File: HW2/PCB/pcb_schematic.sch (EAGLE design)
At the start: 0 parts

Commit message: Started the schematic. Need to add nets.
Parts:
- added C1, C2, C3, C4: (no value), pcb_library:C-US025-025X050
- added C5, C6: (no value), pcb_library:CPOL-USB45181A
- added J1: USB-MB-H, pcb_library:USB-MB-H
- added LED1, LED2: (no value), pcb_library:LED3MM
- added U$1: SLIDE_SWITCH, pcb_library:SLIDE_SWITCH
- added U$2: MCP1702, pcb_library:MCP1702
- added U$3: PIC32MX250F128B, pcb_library:PIC32MX250F128B
- added U$4: PICKIT, pcb_library:PICKIT
- added U$5: J3, pcb_library:J3
- added U$6: J4, pcb_library:J4
- added U$7: 8MHZ, pcb_library:8MHZ

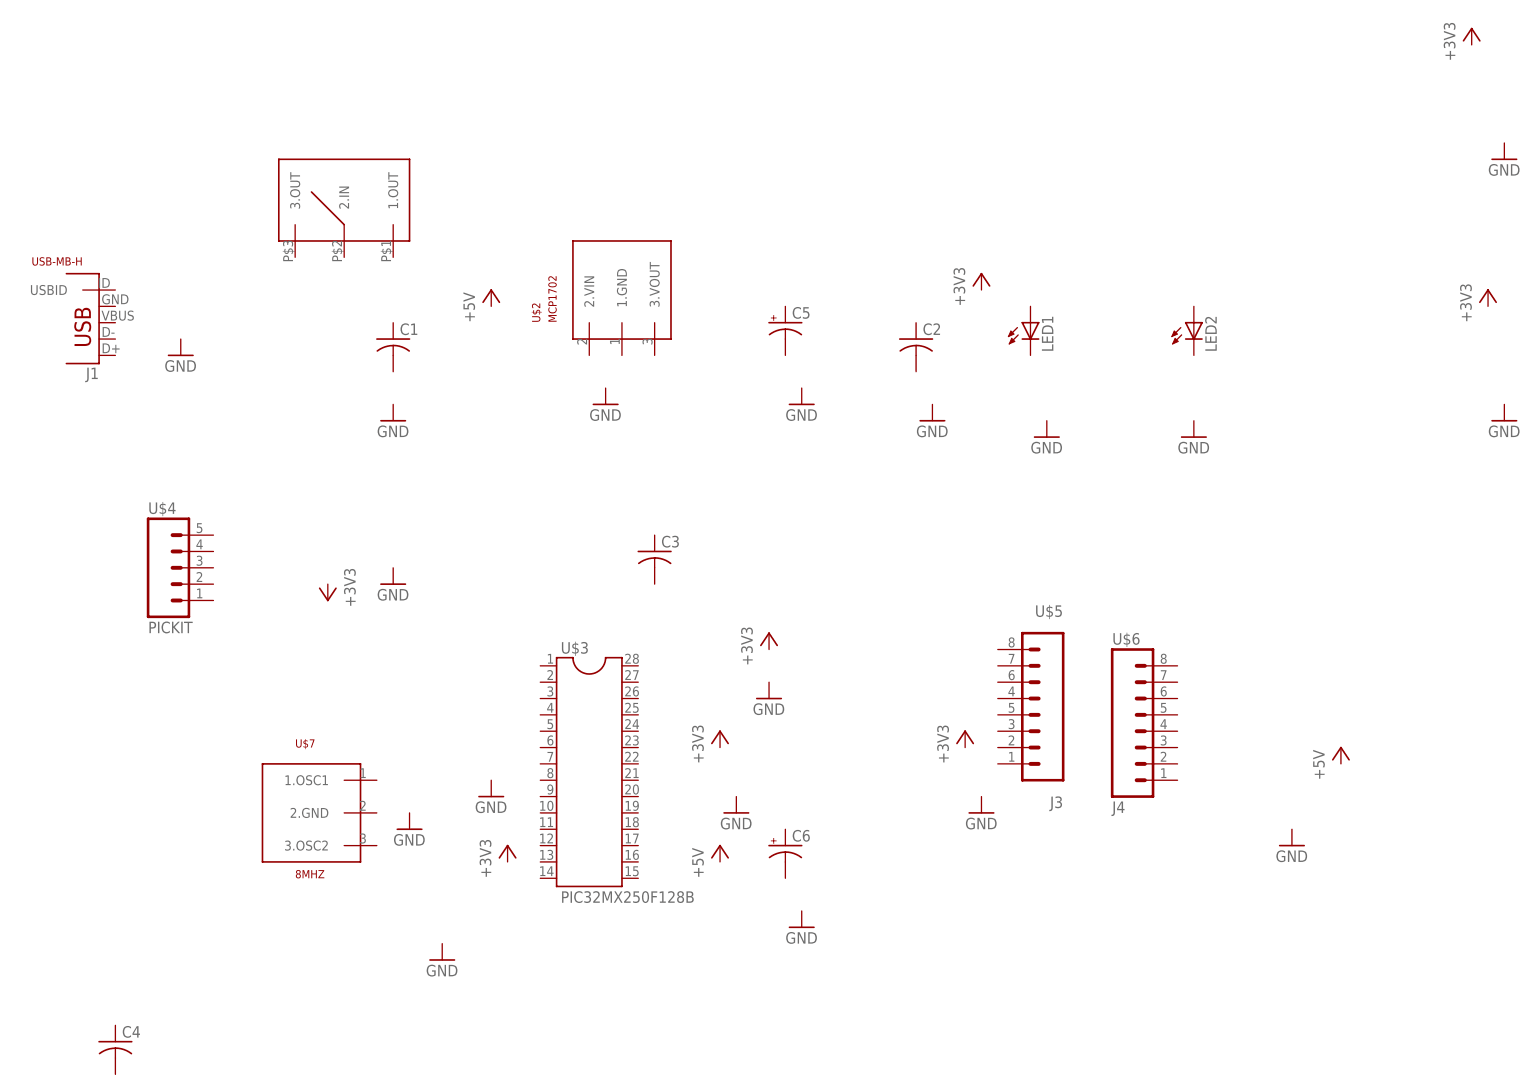
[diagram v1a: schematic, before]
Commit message: Finished a good bit of the schematic.
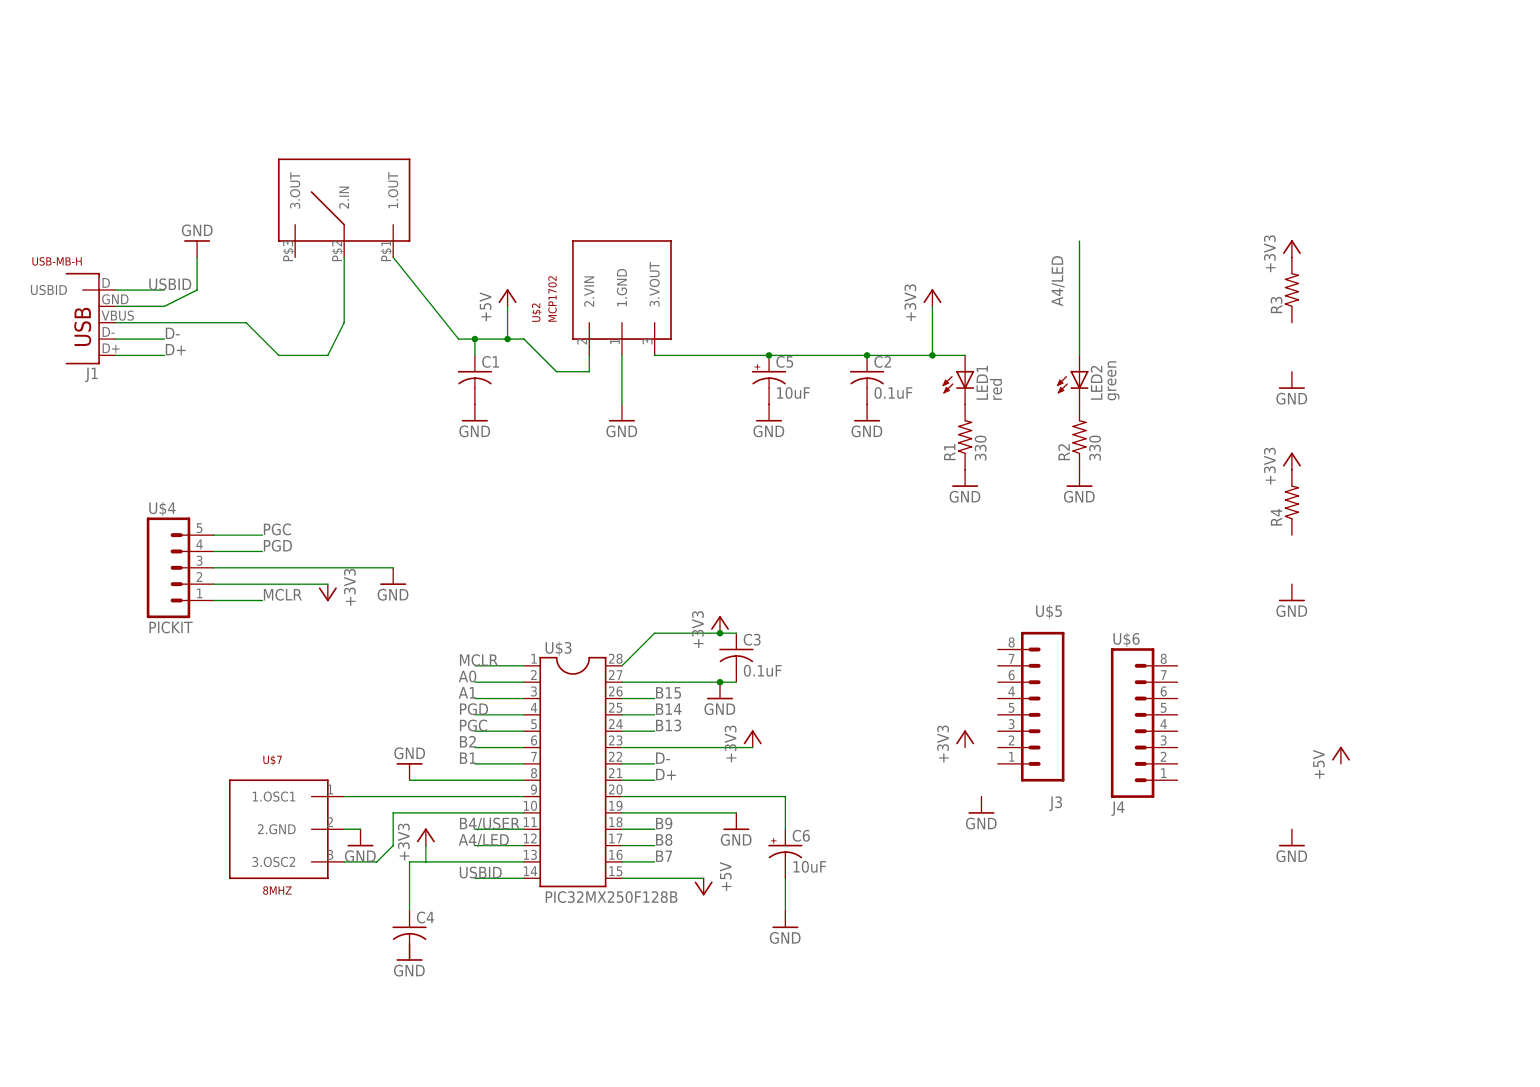
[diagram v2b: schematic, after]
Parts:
- added R1, R2: 330, pcb_library:R-US_0204/7
- added R3, R4: (no value), pcb_library:R-US_0204/7
- C2, C3: value (none) -> 0.1uF
- C5, C6: value (none) -> 10uF
- LED1: value (none) -> red
- LED2: value (none) -> green
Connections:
- new net +3V3: C2.1, C3.1, C4.1, C5.+, LED1.A, R3.2, R4.2, U$2.3.VOUT, U$3.13.VDD, U$3.23.VUSB3V3, U$3.28.AVDD, U$4.2.3V3
- new net +5V: C1.1, U$1.1.OUT, U$2.2.VIN, U$3.15.VBUS
- new net A0: U$3.2.A0
- new net A1: U$3.3.A1
- new net A4/LED: LED2.A, U$3.12.A4/LED
- new net B1: U$3.7.B3
- new net B13: U$3.24.B13
- new net B14: U$3.25.B14
- new net B15: U$3.26.B15
- new net B2: U$3.6.B2
- new net B4/USER: U$3.11.B4/USER
- new net B7: U$3.16.B7
- new net B8: U$3.17.B8
- new net B9: U$3.18.B9
- new net D+: J1.D+, U$3.21.D+/B10
- new net D-: J1.D-, U$3.22.D-/B11
- new net GND: C1.2, C2.2, C3.2, C5.-, C6.-, J1.GND, R1.1, R2.1, U$2.1.GND, U$3.19.VSS, U$3.27.AVSS, U$3.8.GND, U$4.3.GND, U$7.2.GND
- new net MCLR: U$3.1.MCLR, U$4.1.MCLR
- new net N$1: J1.VBUS, U$1.2.IN
- new net N$14: C6.+, U$3.20.VCAP
- new net N$2: LED1.C, R1.2
- new net N$3: LED2.C, R2.2
- new net N$4: U$3.9.OSC1, U$7.1.OSC1
- new net N$5: U$3.10.OSC2, U$7.3.OSC2
- new net PGC: U$3.5.PGC, U$4.5.PGC
- new net PGD: U$3.4.PGD, U$4.4.PGD
- new net USBID: J1.USBID, U$3.14.USBID/B5
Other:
- moved on the sheet: C1, C2, C3, C4, C5, LED1, LED2, U$3, U$7

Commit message: Finished schematic minus the buttons. Not sure what to do about those still.
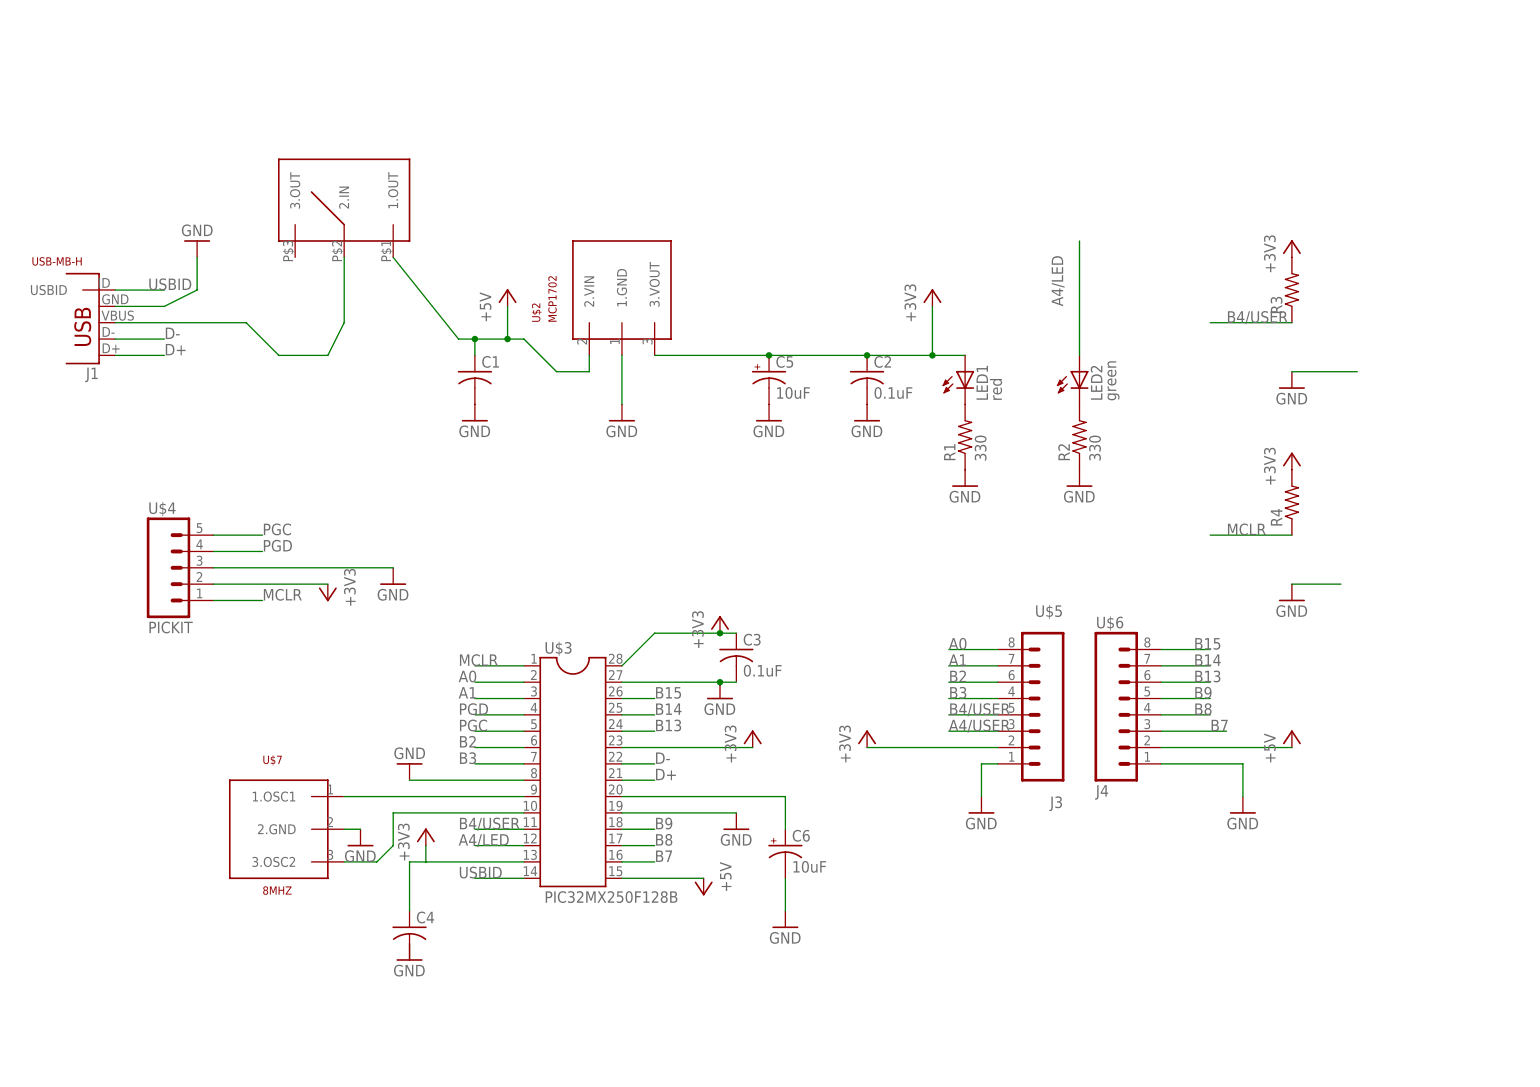
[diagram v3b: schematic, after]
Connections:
- removed net B1: U$3.7.B3
- new net A4/USER: U$5.3.A4/LED
- new net B3: U$3.7.B3, U$5.4.B4/USER
- net +3V3: now also U$5.2.3V3
- net +5V: now also U$6.2.5V
- net A0: now also U$5.8.A0
- net A1: now also U$5.7.A1
- net B13: now also U$6.6.B13
- net B14: now also U$6.7.B14
- net B15: now also U$6.8.B15
- net B2: now also U$5.5.B3
- net B4/USER: now also R3.1, U$5.5
- net B7: now also U$6.3.B7
- net B8: now also U$6.4.B8
- net B9: now also U$6.5.B9
- net GND: now also U$5.1.GND, U$6.1.GND
- net MCLR: now also R4.1
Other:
- moved on the sheet: U$6
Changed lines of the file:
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@@
 <instance part="U$4" gate="G$1" x="-66.04" y="33.02"/>
 <instance part="U$5" gate="G$1" x="71.12" y="12.7"/>
-<instance part="U$6" gate="G$1" x="86.36" y="7.62"/>
+<instance part="U$6" gate="G$1" x="83.82" y="10.16"/>
 <instance part="U$7" gate="G$1" x="-40.64" y="-7.62"/>
 <instance part="P+1" gate="1" x="-12.7" y="76.2"/>
-<instance part="P+2" gate="1" x="116.84" y="5.08"/>
+<instance part="P+2" gate="1" x="109.22" y="7.62"/>
 <instance part="P+3" gate="1" x="17.78" y="-17.78" rot="R180"/>
 <instance part="+3V1" gate="G$1" x="53.34" y="76.2"/>
 <instance part="+3V2" gate="G$1" x="109.22" y="83.82"/>
 <instance part="+3V3" gate="G$1" x="109.22" y="50.8"/>
-<instance part="+3V4" gate="G$1" x="58.42" y="7.62"/>
+<instance part="+3V4" gate="G$1" x="43.18" y="7.62"/>
 <instance part="+3V5" gate="G$1" x="25.4" y="7.62"/>
 <instance part="+3V6" gate="G$1" x="20.32" y="25.4"/>
@@
 <instance part="GND8" gate="1" x="109.22" y="60.96"/>
 <instance part="GND9" gate="1" x="109.22" y="27.94"/>
-<instance part="GND10" gate="1" x="109.22" y="-10.16"/>
+<instance part="GND10" gate="1" x="101.6" y="-5.08"/>
 <instance part="GND11" gate="1" x="60.96" y="-5.08"/>
 <instance part="GND12" gate="1" x="20.32" y="12.7"/>
@@
 <pinref part="GND13" gate="1" pin="GND"/>
 </segment>
+<segment>
+<pinref part="U$5" gate="G$1" pin="1.GND"/>
+<wire x1="63.5" y1="2.54" x2="60.96" y2="2.54" width="0.1524" layer="91"/>
+<pinref part="GND11" gate="1" pin="GND"/>
+<wire x1="60.96" y1="2.54" x2="60.96" y2="-2.54" width="0.1524" layer="91"/>
+</segment>
+<segment>
+<pinref part="U$6" gate="G$1" pin="1.GND"/>
+<wire x1="88.9" y1="2.54" x2="101.6" y2="2.54" width="0.1524" layer="91"/>
+<wire x1="101.6" y1="2.54" x2="101.6" y2="-2.54" width="0.1524" layer="91"/>
+<pinref part="GND10" gate="1" pin="GND"/>
+</segment>
+<segment>
+<pinref part="GND8" gate="1" pin="GND"/>
+<wire x1="119.38" y1="63.5" x2="109.22" y2="63.5" width="0.1524" layer="91"/>
+</segment>
+<segment>
+<pinref part="GND9" gate="1" pin="GND"/>
+<wire x1="116.84" y1="30.48" x2="109.22" y2="30.48" width="0.1524" layer="91"/>
+</segment>
 </net>
 <net name="USBID" class="0">
@@
 <pinref part="P+3" gate="1" pin="+5V"/>
 </segment>
+<segment>
+<pinref part="U$6" gate="G$1" pin="2.5V"/>
+<wire x1="88.9" y1="5.08" x2="109.22" y2="5.08" width="0.1524" layer="91"/>
+<pinref part="P+2" gate="1" pin="+5V"/>
+</segment>
 </net>
 <net name="+3V3" class="0">
@@
 <wire x1="5.08" y1="5.08" x2="25.4" y2="5.08" width="0.1524" layer="91"/>
 </segment>
+<segment>
+<pinref part="U$5" gate="G$1" pin="2.3V3"/>
+<pinref part="+3V4" gate="G$1" pin="+3V3"/>
+<wire x1="63.5" y1="5.08" x2="43.18" y2="5.08" width="0.1524" layer="91"/>
+</segment>
 </net>
 <net name="N$2" class="0">
@@
 <label x="-20.32" y="17.78" size="1.778" layer="95"/>
 </segment>
+<segment>
+<pinref part="R4" gate="G$1" pin="1"/>
+<wire x1="96.52" y1="38.1" x2="109.22" y2="38.1" width="0.1524" layer="91"/>
+<label x="99.06" y="38.1" size="1.778" layer="95"/>
+</segment>
 </net>
 <net name="A0" class="0">
@@
 <label x="-20.32" y="15.24" size="1.778" layer="95"/>
 </segment>
+<segment>
+<pinref part="U$5" gate="G$1" pin="8.A0"/>
+<wire x1="55.88" y1="20.32" x2="63.5" y2="20.32" width="0.1524" layer="91"/>
+<label x="55.88" y="20.32" size="1.778" layer="95"/>
+</segment>
 </net>
 <net name="A1" class="0">
@@
 <label x="-20.32" y="12.7" size="1.778" layer="95"/>
 </segment>
+<segment>
+<pinref part="U$5" gate="G$1" pin="7.A1"/>
+<wire x1="55.88" y1="17.78" x2="63.5" y2="17.78" width="0.1524" layer="91"/>
+<label x="55.88" y="17.78" size="1.778" layer="95"/>
+</segment>
 </net>
 <net name="B2" class="0">
@@
 <label x="-20.32" y="5.08" size="1.778" layer="95"/>
 </segment>
-</net>
-<net name="B1" class="0">
-<segment>
-<pinref part="U$3" gate="G$1" pin="7.B3"/>
-<wire x1="-10.16" y1="2.54" x2="-17.78" y2="2.54" width="0.1524" layer="91"/>
-<label x="-20.32" y="2.54" size="1.778" layer="95"/>
+<segment>
+<pinref part="U$5" gate="G$1" pin="5.B3"/>
+<wire x1="55.88" y1="15.24" x2="63.5" y2="15.24" width="0.1524" layer="91"/>
+<label x="55.88" y="15.24" size="1.778" layer="95"/>
 </segment>
 </net>
@@
 <label x="-20.32" y="-7.62" size="1.778" layer="95"/>
 </segment>
+<segment>
+<pinref part="U$5" gate="G$1" pin="5"/>
+<wire x1="55.88" y1="10.16" x2="63.5" y2="10.16" width="0.1524" layer="91"/>
+<label x="55.88" y="10.16" size="1.778" layer="95"/>
+</segment>
+<segment>
+<pinref part="R3" gate="G$1" pin="1"/>
+<wire x1="96.52" y1="71.12" x2="109.22" y2="71.12" width="0.1524" layer="91"/>
+<label x="99.06" y="71.12" size="1.778" layer="95"/>
+</segment>
 </net>
 <net name="B15" class="0">
@@
 <label x="10.16" y="12.7" size="1.778" layer="95"/>
 </segment>
+<segment>
+<pinref part="U$6" gate="G$1" pin="8.B15"/>
+<wire x1="88.9" y1="20.32" x2="96.52" y2="20.32" width="0.1524" layer="91"/>
+<label x="93.98" y="20.32" size="1.778" layer="95"/>
+</segment>
 </net>
 <net name="B14" class="0">
@@
 <label x="10.16" y="10.16" size="1.778" layer="95"/>
 </segment>
+<segment>
+<pinref part="U$6" gate="G$1" pin="7.B14"/>
+<wire x1="88.9" y1="17.78" x2="96.52" y2="17.78" width="0.1524" layer="91"/>
+<label x="93.98" y="17.78" size="1.778" layer="95"/>
+</segment>
 </net>
 <net name="B13" class="0">
@@
 <wire x1="5.08" y1="7.62" x2="10.16" y2="7.62" width="0.1524" layer="91"/>
 <label x="10.16" y="7.62" size="1.778" layer="95"/>
+</segment>
+<segment>
+<pinref part="U$6" gate="G$1" pin="6.B13"/>
+<wire x1="88.9" y1="15.24" x2="96.52" y2="15.24" width="0.1524" layer="91"/>
+<label x="93.98" y="15.24" size="1.778" layer="95"/>
 </segment>
 </net>
@@
 <label x="10.16" y="-7.62" size="1.778" layer="95"/>
 </segment>
+<segment>
+<pinref part="U$6" gate="G$1" pin="5.B9"/>
+<wire x1="88.9" y1="12.7" x2="96.52" y2="12.7" width="0.1524" layer="91"/>
+<label x="93.98" y="12.7" size="1.778" layer="95"/>
+</segment>
 </net>
 <net name="B8" class="0">
@@
 <label x="10.16" y="-10.16" size="1.778" layer="95"/>
 </segment>
+<segment>
+<pinref part="U$6" gate="G$1" pin="4.B8"/>
+<wire x1="88.9" y1="10.16" x2="96.52" y2="10.16" width="0.1524" layer="91"/>
+<label x="93.98" y="10.16" size="1.778" layer="95"/>
+</segment>
 </net>
 <net name="B7" class="0">
@@
 <label x="10.16" y="-12.7" size="1.778" layer="95"/>
 </segment>
-</net>
+<segment>
+<pinref part="U$6" gate="G$1" pin="3.B7"/>
+<wire x1="88.9" y1="7.62" x2="99.06" y2="7.62" width="0.1524" layer="91"/>
+<label x="96.52" y="7.62" size="1.778" layer="95"/>
+</segment>
+</net>
+<net name="B3" class="0">
+<segment>
+<pinref part="U$5" gate="G$1" pin="4.B4/USER"/>
+<wire x1="55.88" y1="12.7" x2="63.5" y2="12.7" width="0.1524" layer="91"/>
+<label x="55.88" y="12.7" size="1.778" layer="95"/>
+</segment>
+<segment>
+<pinref part="U$3" gate="G$1" pin="7.B3"/>
+<wire x1="-10.16" y1="2.54" x2="-17.78" y2="2.54" width="0.1524" layer="91"/>
+<label x="-20.32" y="2.54" size="1.778" layer="95"/>
+</segment>
+</net>
+<net name="A4/USER" class="0">
+<segment>
+<pinref part="U$5" gate="G$1" pin="3.A4/LED"/>
+<wire x1="63.5" y1="7.62" x2="55.88" y2="7.62" width="0.1524" layer="91"/>
+<label x="55.88" y="7.62" size="1.778" layer="95"/>
+</segment>
+</net>

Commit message: Started board.
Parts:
- C1, C4: value (none) -> 0.1uF
- R3, R4: value (none) -> 10K
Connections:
- removed net A4/USER: U$5.3.A4/LED
- net A4/LED: now also U$5.3.A4/LED
- net GND: now also C4.2
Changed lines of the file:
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@@
 <part name="U$1" library="pcb_library" deviceset="SLIDE_SWITCH" device=""/>
 <part name="U$2" library="pcb_library" deviceset="MCP1702" device=""/>
-<part name="C1" library="pcb_library" deviceset="C-US" device="025-025X050"/>
+<part name="C1" library="pcb_library" deviceset="C-US" device="025-025X050" value="0.1uF"/>
 <part name="C2" library="pcb_library" deviceset="C-US" device="025-025X050" value="0.1uF"/>
 <part name="C3" library="pcb_library" deviceset="C-US" device="025-025X050" value="0.1uF"/>
-<part name="C4" library="pcb_library" deviceset="C-US" device="025-025X050"/>
+<part name="C4" library="pcb_library" deviceset="C-US" device="025-025X050" value="0.1uF"/>
 <part name="C5" library="pcb_library" deviceset="CPOL-US" device="B45181A" value="10uF"/>
 <part name="C6" library="pcb_library" deviceset="CPOL-US" device="B45181A" value="10uF"/>
@@
 <part name="R1" library="pcb_library" deviceset="R-US_" device="0204/7" value="330"/>
 <part name="R2" library="pcb_library" deviceset="R-US_" device="0204/7" value="330"/>
-<part name="R3" library="pcb_library" deviceset="R-US_" device="0204/7"/>
-<part name="R4" library="pcb_library" deviceset="R-US_" device="0204/7"/>
+<part name="R3" library="pcb_library" deviceset="R-US_" device="0204/7" value="10K"/>
+<part name="R4" library="pcb_library" deviceset="R-US_" device="0204/7" value="10K"/>
 </parts>
 <sheets>
@@
 <instance part="GND15" gate="1" x="-27.94" y="2.54" rot="R180"/>
 <instance part="GND16" gate="1" x="-35.56" y="-10.16"/>
-<instance part="GND17" gate="1" x="-27.94" y="-27.94"/>
+<instance part="GND17" gate="1" x="-27.94" y="-30.48"/>
 <instance part="GND18" gate="1" x="-30.48" y="30.48"/>
 <instance part="R1" gate="G$1" x="58.42" y="53.34" rot="R90"/>
@@
 <pinref part="GND9" gate="1" pin="GND"/>
 <wire x1="116.84" y1="30.48" x2="109.22" y2="30.48" width="0.1524" layer="91"/>
+</segment>
+<segment>
+<pinref part="C4" gate="G$1" pin="2"/>
+<pinref part="GND17" gate="1" pin="GND"/>
 </segment>
 </net>
@@
 <pinref part="+3V7" gate="G$1" pin="+3V3"/>
 <wire x1="-25.4" y1="-12.7" x2="-25.4" y2="-10.16" width="0.1524" layer="91"/>
+<junction x="-25.4" y="-12.7"/>
 </segment>
 <segment>
@@
 <label x="-20.32" y="-10.16" size="1.778" layer="95"/>
 </segment>
+<segment>
+<pinref part="U$5" gate="G$1" pin="3.A4/LED"/>
+<wire x1="63.5" y1="7.62" x2="55.88" y2="7.62" width="0.1524" layer="91"/>
+<label x="55.88" y="7.62" size="1.778" layer="95"/>
+</segment>
 </net>
 <net name="PGC" class="0">
@@
 </segment>
 </net>
-<net name="A4/USER" class="0">
-<segment>
-<pinref part="U$5" gate="G$1" pin="3.A4/LED"/>
-<wire x1="63.5" y1="7.62" x2="55.88" y2="7.62" width="0.1524" layer="91"/>
-<label x="55.88" y="7.62" size="1.778" layer="95"/>
-</segment>
-</net>
